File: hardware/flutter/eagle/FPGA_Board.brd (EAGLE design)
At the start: 100 x 77 mm, 81 parts, among them IC1 AT45DB161D-SU, IC2 MEGA8-AI, IC3 MAX481CSA, Q1 8Mhz, U2 XC3S50AVQ100, X1 BU-SMA-V, X2 MINI-USB-32005-201

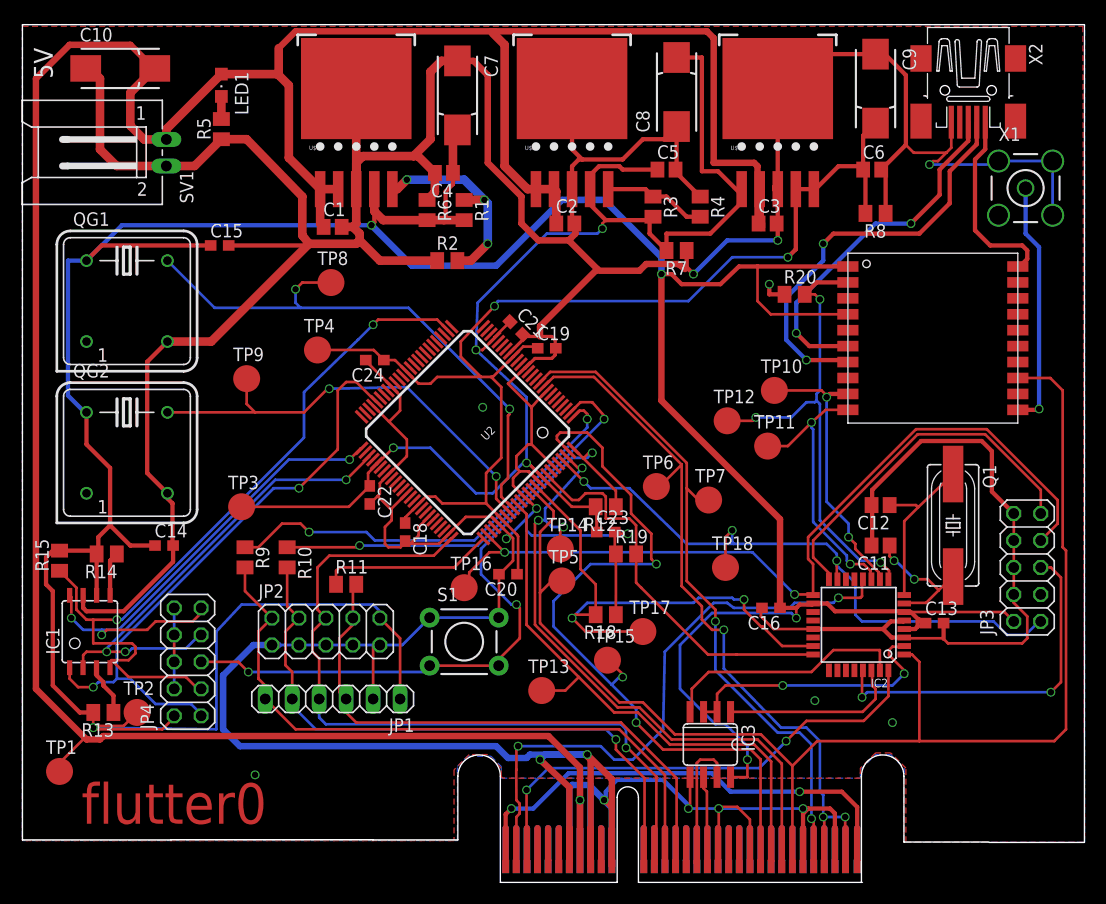
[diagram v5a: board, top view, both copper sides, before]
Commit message: added alternative pads for an oscillator with other pinlayout in flutter0 layout of oscillator was added to hgg.lbr
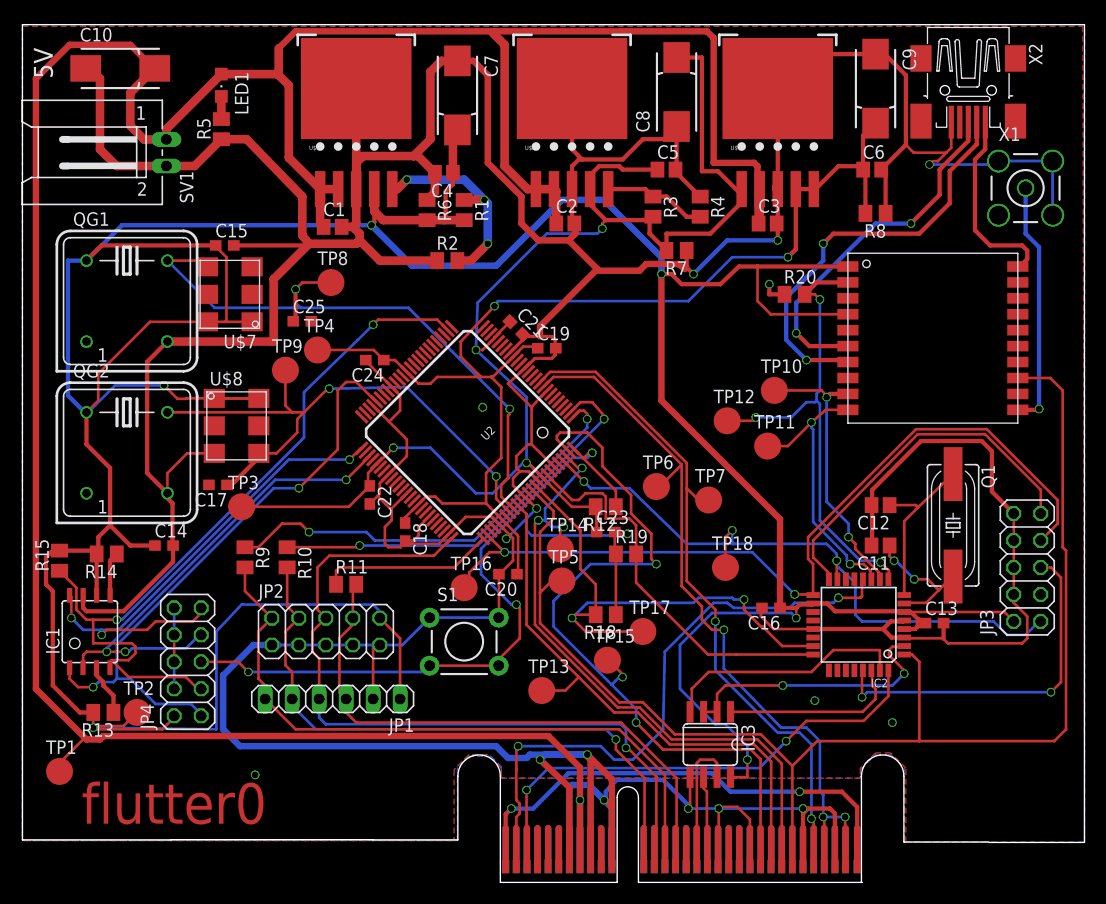
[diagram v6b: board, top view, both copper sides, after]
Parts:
- added C17, C25: (no value), resistor:C0603
- added U$7, U$8: OSCILLATOR, hgg:OSCILLATOR
- Q1: device crystal:HC49UP -> crystal:SM49
- moved TP9 3.74 mm to (24.8, 47.5)
- moved C15 0.48 mm to (19.1, 59.2)
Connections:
- net FPGA_SPI_CLOCK: now also C17.1, U$8.OUTPUT
- net GND: now also C17.2, C25.2, U$7.GND, U$8.GND
- net TIMING_CLK: now also C25.1, U$7.OUTPUT
- net VCC3.3: now also U$7.E/D, U$7.VDD, U$8.E/D, U$8.VDD
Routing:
- net VCC3.3: track 354.1 -> 405.1 mm, vias 5 -> 6
- net FPGA_SPI_CLOCK: track 42.8 -> 54.7 mm
- net GND: track 705.6 -> 715.7 mm
- net TIMING_CLK: track 53.7 -> 60.7 mm
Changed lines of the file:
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@@
 </element>
 <element name="JP3" library="pinhead" package="2X05" value="ISP" x="94.615" y="28.8925" rot="R90"/>
-<element name="Q1" library="crystal" package="HC49UP" value="8Mhz" x="87.63" y="32.86125" rot="R270">
+<element name="Q1" library="crystal" package="SM49" value="8Mhz" x="87.63" y="32.86125" rot="R270">
 <attribute name="OC_NEWARK" value="unknown" x="87.63" y="32.86125" size="1.778" layer="27" rot="R270" display="off"/>
 <attribute name="MPN" value="" x="87.63" y="32.86125" size="1.778" layer="27" rot="R270" display="off"/>
@@
 <element name="C13" library="resistor" package="C0603" value="" x="85.88375" y="23.65375"/>
 <element name="C14" library="resistor" package="C0603" value="" x="13.335" y="30.95625"/>
-<element name="C15" library="resistor" package="C0603" value="" x="18.57375" y="59.21375"/>
+<element name="C15" library="resistor" package="C0603" value="" x="19.05" y="59.21375"/>
 <element name="C16" library="resistor" package="C0603" value="" x="70.485" y="25.0825" rot="R180"/>
 <element name="C18" library="resistor" package="C0603" value="" x="36.03625" y="32.22625" rot="R270"/>
@@
 <attribute name="TP_SIGNAL_NAME" value="" x="29.05125" y="55.72125" size="1.778" layer="27" display="off"/>
 </element>
-<element name="TP9" library="testpad" package="B2,54" value="TPB2,54" x="21.11375" y="46.6725">
-<attribute name="TP_SIGNAL_NAME" value="" x="21.11375" y="46.6725" size="1.778" layer="27" display="off"/>
+<element name="TP9" library="testpad" package="B2,54" value="TPB2,54" x="24.765" y="47.46625">
+<attribute name="TP_SIGNAL_NAME" value="" x="24.765" y="47.46625" size="1.778" layer="27" display="off"/>
 </element>
 <element name="TP10" library="testpad" package="B2,54" value="TPB2,54" x="70.8025" y="45.56125">
@@
 </element>
 <element name="JP4" library="pinhead" package="2X05" value="ISP" x="15.5575" y="20.0025" rot="R90"/>
+<element name="U$7" library="hgg" package="OSCILLATOR" value="OSCILLATOR" x="19.52625" y="54.61" rot="R180"/>
+<element name="U$8" library="hgg" package="OSCILLATOR" value="OSCILLATOR" x="20.16125" y="42.2275"/>
+<element name="C17" library="resistor" package="C0603" value="" x="18.415" y="36.67125" rot="R180"/>
+<element name="C25" library="resistor" package="C0603" value="" x="26.3525" y="52.07"/>
 </elements>
 <signals>
@@
 <wire x1="39.055" y1="57.785" x2="33.655" y2="57.785" width="0.8128" layer="1"/>
 <wire x1="33.655" y1="57.785" x2="31.75" y2="59.69" width="0.8128" layer="1"/>
-<wire x1="13.6525" y1="50.165" x2="17.78" y2="50.165" width="0.8128" layer="1"/>
-<wire x1="17.78" y1="50.165" x2="26.908125" y2="59.293125" width="0.8128" layer="1"/>
+<wire x1="13.6525" y1="50.165" x2="23.65375" y2="50.165" width="0.8128" layer="1"/>
+<wire x1="23.65375" y1="50.165" x2="23.65375" y2="56.03875" width="0.8128" layer="1"/>
+<wire x1="23.65375" y1="56.03875" x2="26.908125" y2="59.293125" width="0.8128" layer="1"/>
 <wire x1="26.908125" y1="59.293125" x2="26.9875" y2="59.3725" width="0.8128" layer="1"/>
 <wire x1="5.715" y1="26.264" x2="5.715" y2="25.0825" width="0.4064" layer="1"/>
@@
 <wire x1="86.73375" y1="23.65375" x2="86.73375" y2="22.16875" width="0.4064" layer="1"/>
 <wire x1="14.185" y1="30.95625" x2="14.185" y2="29.425" width="0.4064" layer="1"/>
-<wire x1="19.42375" y1="59.21375" x2="26.82875" y2="59.21375" width="0.4064" layer="1"/>
+<wire x1="19.9" y1="59.21375" x2="26.82875" y2="59.21375" width="0.4064" layer="1"/>
 <wire x1="26.82875" y1="59.21375" x2="26.908125" y2="59.293125" width="0.4064" layer="1"/>
 <wire x1="74.4474" y1="23.095" x2="81.03875" y2="23.095" width="0.4064" layer="1"/>
@@
 <via x="70.32625" y="55.5625" extent="1-16" drill="0.6" shape="octagon"/>
 <wire x1="70.32625" y1="55.5625" x2="70.32625" y2="55.40375" width="0.4064" layer="16"/>
+<contactref element="U$7" pad="GND"/>
+<contactref element="U$8" pad="GND"/>
+<contactref element="C25" pad="2"/>
+<contactref element="C17" pad="2"/>
+<wire x1="13.6525" y1="35.8775" x2="13.6525" y2="37.76875" width="0.254" layer="1"/>
+<wire x1="13.6525" y1="37.76875" x2="14.76375" y2="38.89375" width="0.254" layer="1"/>
+<wire x1="14.76375" y1="38.89375" x2="15.5075" y2="39.6375" width="0.254" layer="1"/>
+<wire x1="15.5075" y1="39.6375" x2="18.06125" y2="39.6375" width="0.254" layer="1"/>
+<wire x1="34.414665625" y1="37.6327" x2="34.44875" y2="37.62375" width="0" layer="19" extent="1-1"/>
 </signal>
 <signal name="+5V">
@@
 <wire x1="12.485" y1="30.95625" x2="10.16" y2="30.95625" width="0.4064" layer="1"/>
 <wire x1="10.16" y1="30.95625" x2="8.255" y2="32.86125" width="0.4064" layer="1"/>
-<wire x1="17.72375" y1="59.21375" x2="7.46125" y2="59.21375" width="0.4064" layer="1"/>
+<wire x1="18.2" y1="59.21375" x2="7.46125" y2="59.21375" width="0.4064" layer="1"/>
 <wire x1="7.46125" y1="59.21375" x2="6.0325" y2="57.785" width="0.4064" layer="1"/>
 <contactref element="IC2" pad="18"/>
@@
 <wire x1="13.17625" y1="13.6525" x2="6.82625" y2="13.6525" width="0.254" layer="1"/>
 <wire x1="6.82625" y1="13.6525" x2="6.6675" y2="13.81125" width="0.254" layer="1"/>
+<contactref element="U$7" pad="E/D"/>
+<contactref element="U$7" pad="VDD"/>
+<contactref element="U$8" pad="E/D"/>
+<contactref element="U$8" pad="VDD"/>
+<wire x1="17.42625" y1="52.02" x2="19.05" y2="52.02" width="0.254" layer="1"/>
+<wire x1="19.20875" y1="52.02" x2="21.62625" y2="52.02" width="0.254" layer="1"/>
+<wire x1="22.26125" y1="44.8175" x2="18.06125" y2="44.8175" width="0.254" layer="1"/>
+<wire x1="18.2" y1="59.21375" x2="18.2" y2="59.11125" width="0.254" layer="1"/>
+<wire x1="18.2" y1="59.11125" x2="19.20875" y2="58.1025" width="0.254" layer="1"/>
+<wire x1="19.20875" y1="58.1025" x2="19.20875" y2="52.02" width="0.254" layer="1"/>
+<wire x1="19.20875" y1="52.02" x2="19.05" y2="52.02" width="0.254" layer="1"/>
+<wire x1="22.26125" y1="44.8175" x2="15.44875" y2="44.8175" width="0.254" layer="1"/>
+<wire x1="15.44875" y1="44.8175" x2="15.39875" y2="44.7675" width="0.254" layer="1"/>
+<wire x1="15.39875" y1="44.7675" x2="14.605" y2="44.7675" width="0.254" layer="1"/>
+<wire x1="14.605" y1="44.7675" x2="13.335" y2="46.0375" width="0.254" layer="1"/>
+<via x="13.335" y="46.0375" extent="1-16" drill="0.6" shape="octagon"/>
+<wire x1="13.335" y1="46.0375" x2="8.73125" y2="46.0375" width="0.254" layer="16"/>
+<wire x1="8.73125" y1="46.0375" x2="6.0325" y2="43.33875" width="0.254" layer="16"/>
+<wire x1="6.0325" y1="43.33875" x2="6.0325" y2="43.4975" width="0.254" layer="16"/>
+<wire x1="17.42625" y1="52.02" x2="12.015" y2="52.02" width="0.254" layer="1"/>
+<wire x1="12.015" y1="52.02" x2="7.14375" y2="47.14875" width="0.254" layer="1"/>
+<wire x1="7.14375" y1="47.14875" x2="7.14375" y2="44.60875" width="0.254" layer="1"/>
+<wire x1="7.14375" y1="44.60875" x2="6.0325" y2="43.4975" width="0.254" layer="1"/>
 <wire x1="83.02625" y1="24.765" x2="83.0326" y2="24.695" width="0" layer="19" extent="1-1"/>
 </signal>
@@
 <wire x1="44.60875" y1="37.465" x2="44.60875" y2="35.3582125" width="0.254" layer="1"/>
 <wire x1="44.60875" y1="35.3582125" x2="45.869796875" y2="34.097165625" width="0.254" layer="1"/>
-<wire x1="13.6525" y1="43.4975" x2="21.9075" y2="43.4975" width="0.254" layer="1"/>
-<wire x1="21.9075" y1="43.4975" x2="26.51125" y2="43.4975" width="0.254" layer="1"/>
+<wire x1="13.6525" y1="43.4975" x2="25.4" y2="43.4975" width="0.254" layer="1"/>
+<wire x1="25.4" y1="43.4975" x2="26.51125" y2="43.4975" width="0.254" layer="1"/>
 <wire x1="26.51125" y1="43.4975" x2="28.73375" y2="45.72" width="0.254" layer="1"/>
 <wire x1="28.73375" y1="45.72" x2="28.8925" y2="45.72" width="0.254" layer="1"/>
@@
 <wire x1="28.8925" y1="45.72" x2="36.195" y2="45.87875" width="0.254" layer="16"/>
 <contactref element="TP9" pad="TP"/>
-<wire x1="21.11375" y1="46.6725" x2="21.11375" y2="44.29125" width="0.254" layer="1"/>
-<wire x1="21.11375" y1="44.29125" x2="21.9075" y2="43.4975" width="0.254" layer="1"/>
+<wire x1="24.765" y1="47.46625" x2="24.765" y2="44.1325" width="0.254" layer="1"/>
+<wire x1="24.765" y1="44.1325" x2="25.4" y2="43.4975" width="0.254" layer="1"/>
+<contactref element="U$8" pad="OUTPUT"/>
+<contactref element="C17" pad="1"/>
+<wire x1="19.265" y1="36.67125" x2="19.1525" y2="36.6875" width="0.4064" layer="1"/>
+<wire x1="19.1525" y1="36.6875" x2="19.70125" y2="36.6875" width="0.4064" layer="1"/>
+<wire x1="19.70125" y1="36.6875" x2="22.225" y2="39.21125" width="0.4064" layer="1"/>
+<wire x1="22.225" y1="39.21125" x2="22.26125" y2="39.6375" width="0.4064" layer="1"/>
+<wire x1="22.26125" y1="39.6375" x2="23.92125" y2="39.6375" width="0.254" layer="1"/>
+<wire x1="23.92125" y1="39.6375" x2="25.87625" y2="41.5925" width="0.254" layer="1"/>
+<wire x1="25.87625" y1="41.5925" x2="25.87625" y2="42.8625" width="0.254" layer="1"/>
+<wire x1="25.87625" y1="42.8625" x2="26.51125" y2="43.4975" width="0.254" layer="1"/>
 </signal>
 <signal name="MISO_EEPROM">
@@
 <wire x1="25.7175" y1="55.08625" x2="25.7175" y2="53.81625" width="0.254" layer="16"/>
 <wire x1="25.7175" y1="53.81625" x2="26.19375" y2="53.34" width="0.254" layer="16"/>
+<contactref element="U$7" pad="OUTPUT"/>
+<contactref element="C25" pad="1"/>
+<wire x1="25.5025" y1="52.07" x2="25.7175" y2="52.3875" width="0.4064" layer="1"/>
+<wire x1="25.7175" y1="52.3875" x2="25.7175" y2="55.08625" width="0.4064" layer="1"/>
+<wire x1="13.6525" y1="57.785" x2="16.365" y2="57.785" width="0.254" layer="1"/>
+<wire x1="16.365" y1="57.785" x2="17.42625" y2="57.2" width="0.254" layer="1"/>
 </signal>
 </signals>
